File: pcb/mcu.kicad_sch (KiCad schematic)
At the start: 3 parts

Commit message: more mcu
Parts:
- added C? (x3): C, symbol Device:C
- added J?: pin_headers, symbol Carl_symboler:pin_headers
- added Y?: Crystal_GND24, symbol Device:Crystal_GND24
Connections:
- net GND: now also U?.B10 (USB_VREGI), U?.B8 (USB_VBUS), C?.2, C?.2, C?.2, Y?.2, Y?.4
- net +3.3V: now reaches U?.K8 (AVDD_2)
- net +3.3V: now also U?.K9 (AVDD_1), U?.L10 (AVDD_0)
- net at U?.L8 (PB13): now also C?.1, Y?.3
- net at U?.L9 (PB14): now also C?.1, Y?.1
- net må vi spesifisere noe her?: now reaches U?.F11 (DECOUPLE)
- net må vi spesifisere noe her?: now also C?.1

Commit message: idk
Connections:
- net +3.3V: now also U?.D5 (IOVDD_6), U?.D7 (IOVDD_5), U?.G4 (IOVDD_0), U?.G8 (IOVDD_4), U?.H7 (IOVDD_3), U?.L4 (IOVDD_1)
- no-connect marks 9 -> 10
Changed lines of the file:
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@@
   (junction (at 137.16 74.93) (diameter 0) (color 0 0 0 0)
   )
+  (junction (at 113.03 119.38) (diameter 0) (color 0 0 0 0)
+  )
   (junction (at 137.16 73.66) (diameter 0) (color 0 0 0 0)
   )
+  (junction (at 179.07 62.23) (diameter 0) (color 0 0 0 0)
+  )
   (junction (at 247.65 72.39) (diameter 0) (color 0 0 0 0)
   )
@@
   (junction (at 247.65 69.85) (diameter 0) (color 0 0 0 0)
   )
+  (junction (at 179.07 59.69) (diameter 0) (color 0 0 0 0)
+  )
+  (junction (at 173.99 48.26) (diameter 0) (color 0 0 0 0)
+  )
   (junction (at 38.1 96.52) (diameter 0) (color 0 0 0 0)
   )
   (junction (at 137.16 68.58) (diameter 0) (color 0 0 0 0)
+  )
+  (junction (at 110.49 58.42) (diameter 0) (color 0 0 0 0)
+  )
+  (junction (at 110.49 48.26) (diameter 0) (color 0 0 0 0)
   )
   (no_connect (at 152.4 69.85))
@@
   (no_connect (at 142.24 69.85))
   (no_connect (at 152.4 73.66))
+  (no_connect (at 44.45 104.14))
+  (bus_entry (at 214.63 99.06) (size 2.54 2.54)
+    (stroke (width 0) (type default) (color 0 0 0 0))
+  )
   (wire (pts (xy 247.65 72.39) (xy 247.65 105.41))
     (stroke (width 0) (type default) (color 0 0 0 0))
@@
     (stroke (width 0) (type default) (color 0 0 0 0))
   )
+  (wire (pts (xy 179.07 62.23) (xy 179.07 59.69))
+    (stroke (width 0) (type default) (color 0 0 0 0))
+  )
+  (wire (pts (xy 110.49 58.42) (xy 110.49 48.26))
+    (stroke (width 0) (type default) (color 0 0 0 0))
+  )
   (wire (pts (xy 44.45 127) (xy 36.83 127))
     (stroke (width 0) (type default) (color 0 0 0 0))
@@
     (stroke (width 0) (type default) (color 0 0 0 0))
   )
+  (wire (pts (xy 179.07 59.69) (xy 186.69 59.69))
+    (stroke (width 0) (type default) (color 0 0 0 0))
+  )
   (wire (pts (xy 105.41 66.04) (xy 133.35 66.04))
     (stroke (width 0) (type default) (color 0 0 0 0))
@@
     (stroke (width 0) (type default) (color 0 0 0 0))
   )
+  (wire (pts (xy 179.07 90.17) (xy 179.07 62.23))
+    (stroke (width 0) (type default) (color 0 0 0 0))
+  )
   (wire (pts (xy 127 88.9) (xy 127 49.53))
     (stroke (width 0) (type default) (color 0 0 0 0))
@@
     (stroke (width 0) (type default) (color 0 0 0 0))
   )
+  (wire (pts (xy 243.84 36.83) (xy 173.99 36.83))
+    (stroke (width 0) (type default) (color 0 0 0 0))
+  )
   (wire (pts (xy 237.49 105.41) (xy 247.65 105.41))
     (stroke (width 0) (type default) (color 0 0 0 0))
@@
     (stroke (width 0) (type default) (color 0 0 0 0))
   )
+  (wire (pts (xy 119.38 119.38) (xy 119.38 116.84))
+    (stroke (width 0) (type default) (color 0 0 0 0))
+  )
   (wire (pts (xy 137.16 72.39) (xy 142.24 72.39))
     (stroke (width 0) (type default) (color 0 0 0 0))
@@
     (stroke (width 0) (type default) (color 0 0 0 0))
   )
+  (wire (pts (xy 179.07 59.69) (xy 179.07 48.26))
+    (stroke (width 0) (type default) (color 0 0 0 0))
+  )
   (wire (pts (xy 264.16 95.25) (xy 273.05 95.25))
     (stroke (width 0) (type default) (color 0 0 0 0))
@@
     (stroke (width 0) (type default) (color 0 0 0 0))
   )
+  (wire (pts (xy 186.69 90.17) (xy 179.07 90.17))
+    (stroke (width 0) (type default) (color 0 0 0 0))
+  )
   (wire (pts (xy 156.21 146.05) (xy 156.21 66.04))
     (stroke (width 0) (type default) (color 0 0 0 0))
@@
     (stroke (width 0) (type default) (color 0 0 0 0))
   )
+  (wire (pts (xy 110.49 48.26) (xy 110.49 45.72))
+    (stroke (width 0) (type default) (color 0 0 0 0))
+  )
   (wire (pts (xy 105.41 88.9) (xy 127 88.9))
     (stroke (width 0) (type default) (color 0 0 0 0))
@@
     (stroke (width 0) (type default) (color 0 0 0 0))
   )
+  (wire (pts (xy 105.41 58.42) (xy 110.49 58.42))
+    (stroke (width 0) (type default) (color 0 0 0 0))
+  )
+  (wire (pts (xy 105.41 63.5) (xy 110.49 63.5))
+    (stroke (width 0) (type default) (color 0 0 0 0))
+  )
+  (wire (pts (xy 243.84 90.17) (xy 243.84 36.83))
+    (stroke (width 0) (type default) (color 0 0 0 0))
+  )
   (wire (pts (xy 44.45 101.6) (xy 38.1 101.6))
     (stroke (width 0) (type default) (color 0 0 0 0))
   )
+  (wire (pts (xy 179.07 62.23) (xy 186.69 62.23))
+    (stroke (width 0) (type default) (color 0 0 0 0))
+  )
   (wire (pts (xy 273.05 95.25) (xy 273.05 73.66))
     (stroke (width 0) (type default) (color 0 0 0 0))
@@
     (stroke (width 0) (type default) (color 0 0 0 0))
   )
+  (wire (pts (xy 237.49 90.17) (xy 243.84 90.17))
+    (stroke (width 0) (type default) (color 0 0 0 0))
+  )
   (wire (pts (xy 137.16 64.77) (xy 142.24 64.77))
     (stroke (width 0) (type default) (color 0 0 0 0))
@@
     (stroke (width 0) (type default) (color 0 0 0 0))
   )
+  (wire (pts (xy 173.99 48.26) (xy 110.49 48.26))
+    (stroke (width 0) (type default) (color 0 0 0 0))
+  )
   (wire (pts (xy 242.57 34.29) (xy 242.57 64.77))
     (stroke (width 0) (type default) (color 0 0 0 0))
@@
     (stroke (width 0) (type default) (color 0 0 0 0))
   )
+  (wire (pts (xy 173.99 36.83) (xy 173.99 48.26))
+    (stroke (width 0) (type default) (color 0 0 0 0))
+  )
+  (wire (pts (xy 110.49 63.5) (xy 110.49 58.42))
+    (stroke (width 0) (type default) (color 0 0 0 0))
+  )
   (wire (pts (xy 133.35 66.04) (xy 133.35 50.8))
     (stroke (width 0) (type default) (color 0 0 0 0))
@@
     (stroke (width 0) (type default) (color 0 0 0 0))
   )
+  (wire (pts (xy 179.07 48.26) (xy 173.99 48.26))
+    (stroke (width 0) (type default) (color 0 0 0 0))
+  )
   (wire (pts (xy 273.05 73.66) (xy 241.3 73.66))
     (stroke (width 0) (type default) (color 0 0 0 0))
@@
   )
   (wire (pts (xy 154.94 49.53) (xy 154.94 64.77))
+    (stroke (width 0) (type default) (color 0 0 0 0))
+  )
+  (wire (pts (xy 113.03 119.38) (xy 119.38 119.38))
     (stroke (width 0) (type default) (color 0 0 0 0))
   )
@@
     )
     (property "Datasheet" "" (id 3) (at 247.65 68.58 0)
+      (effects (font (size 1.27 1.27)) hide)
+    )
+    (pin "1")
+  )
+  (symbol (lib_id "power:PWR_FLAG") (at 119.38 116.84 0) (unit 1)
+    (in_bom yes) (on_board yes) (fields_autoplaced)
+    (property "Reference" "#FLG?" (id 0) (at 119.38 114.935 0)
+      (effects (font (size 1.27 1.27)) hide)
+    )
+    (property "Value" "" (id 1) (at 119.38 111.76 0))
+    (property "Footprint" "" (id 2) (at 119.38 116.84 0)
+      (effects (font (size 1.27 1.27)) hide)
+    )
+    (property "Datasheet" "~" (id 3) (at 119.38 116.84 0)
       (effects (font (size 1.27 1.27)) hide)
     )
@@
       (effects (font (size 1.27 1.27)) hide)
     )
+    (pin "1")
+  )
+  (symbol (lib_id "power:+3.3V") (at 110.49 45.72 0) (unit 1)
+    (in_bom yes) (on_board yes) (fields_autoplaced)
+    (property "Reference" "#PWR?" (id 0) (at 110.49 49.53 0)
+      (effects (font (size 1.27 1.27)) hide)
+    )
+    (property "Value" "" (id 1) (at 110.49 40.64 0))
+    (property "Footprint" "" (id 2) (at 110.49 45.72 0)
+      (effects (font (size 1.27 1.27)) hide)
+    )
+    (property "Datasheet" "" (id 3) (at 110.49 45.72 0)
+      (effects (font (size 1.27 1.27)) hide)
+    )

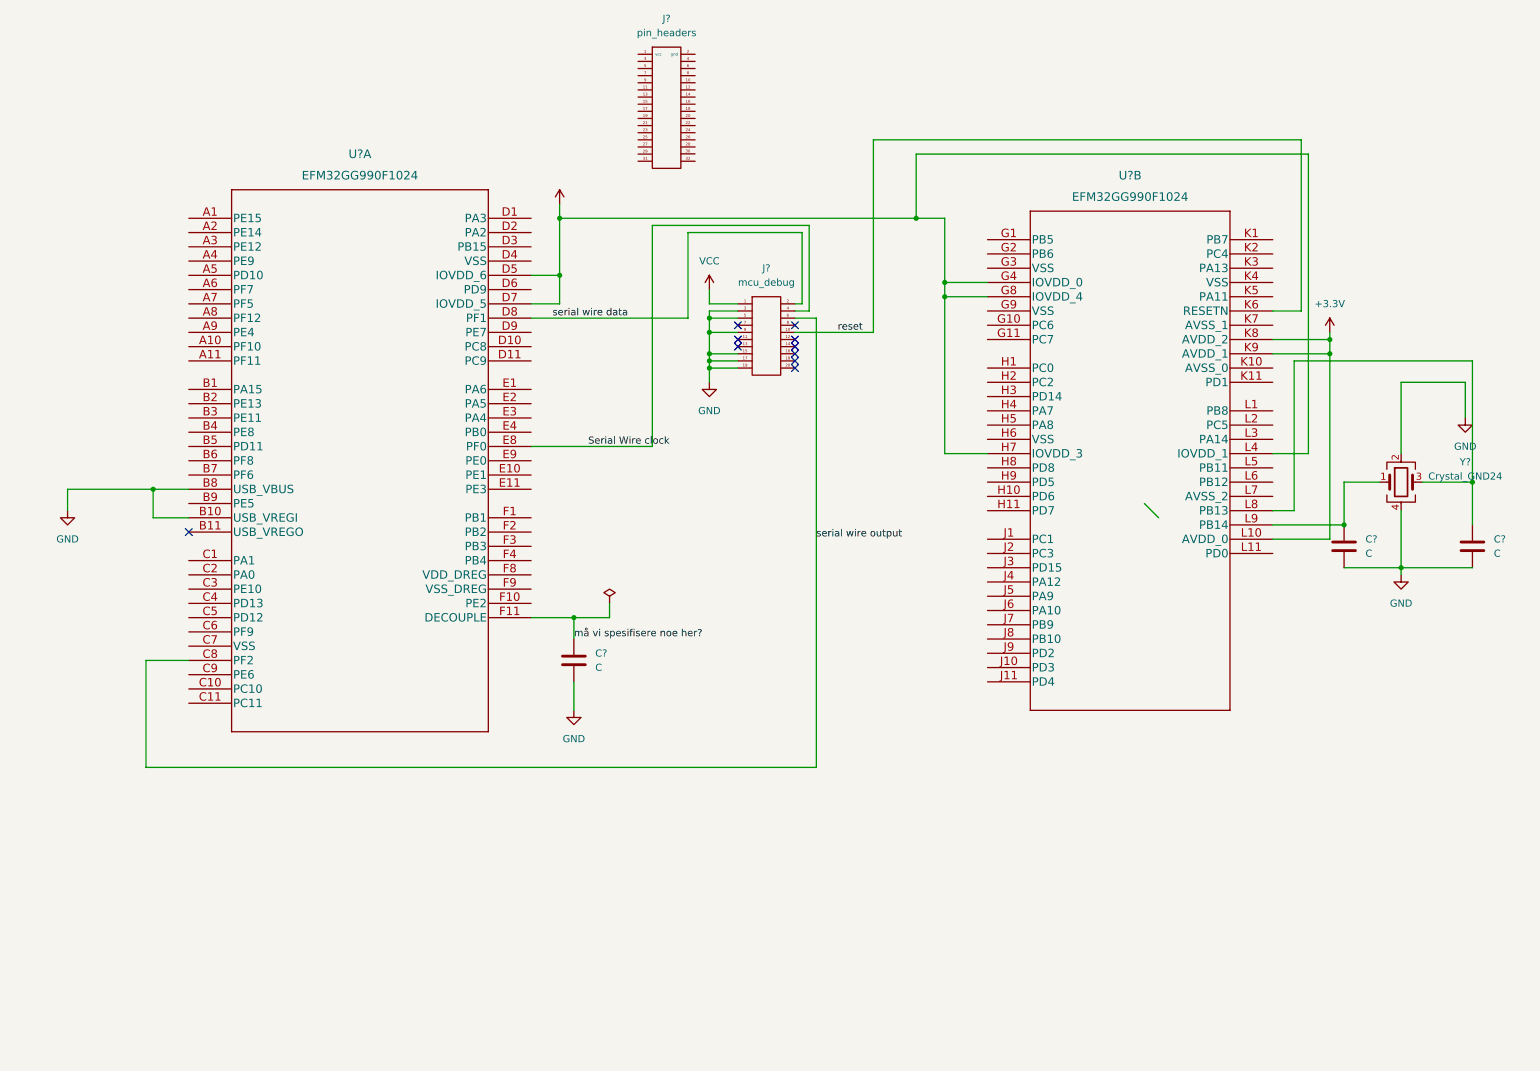
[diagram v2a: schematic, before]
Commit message: add global labels and footprint
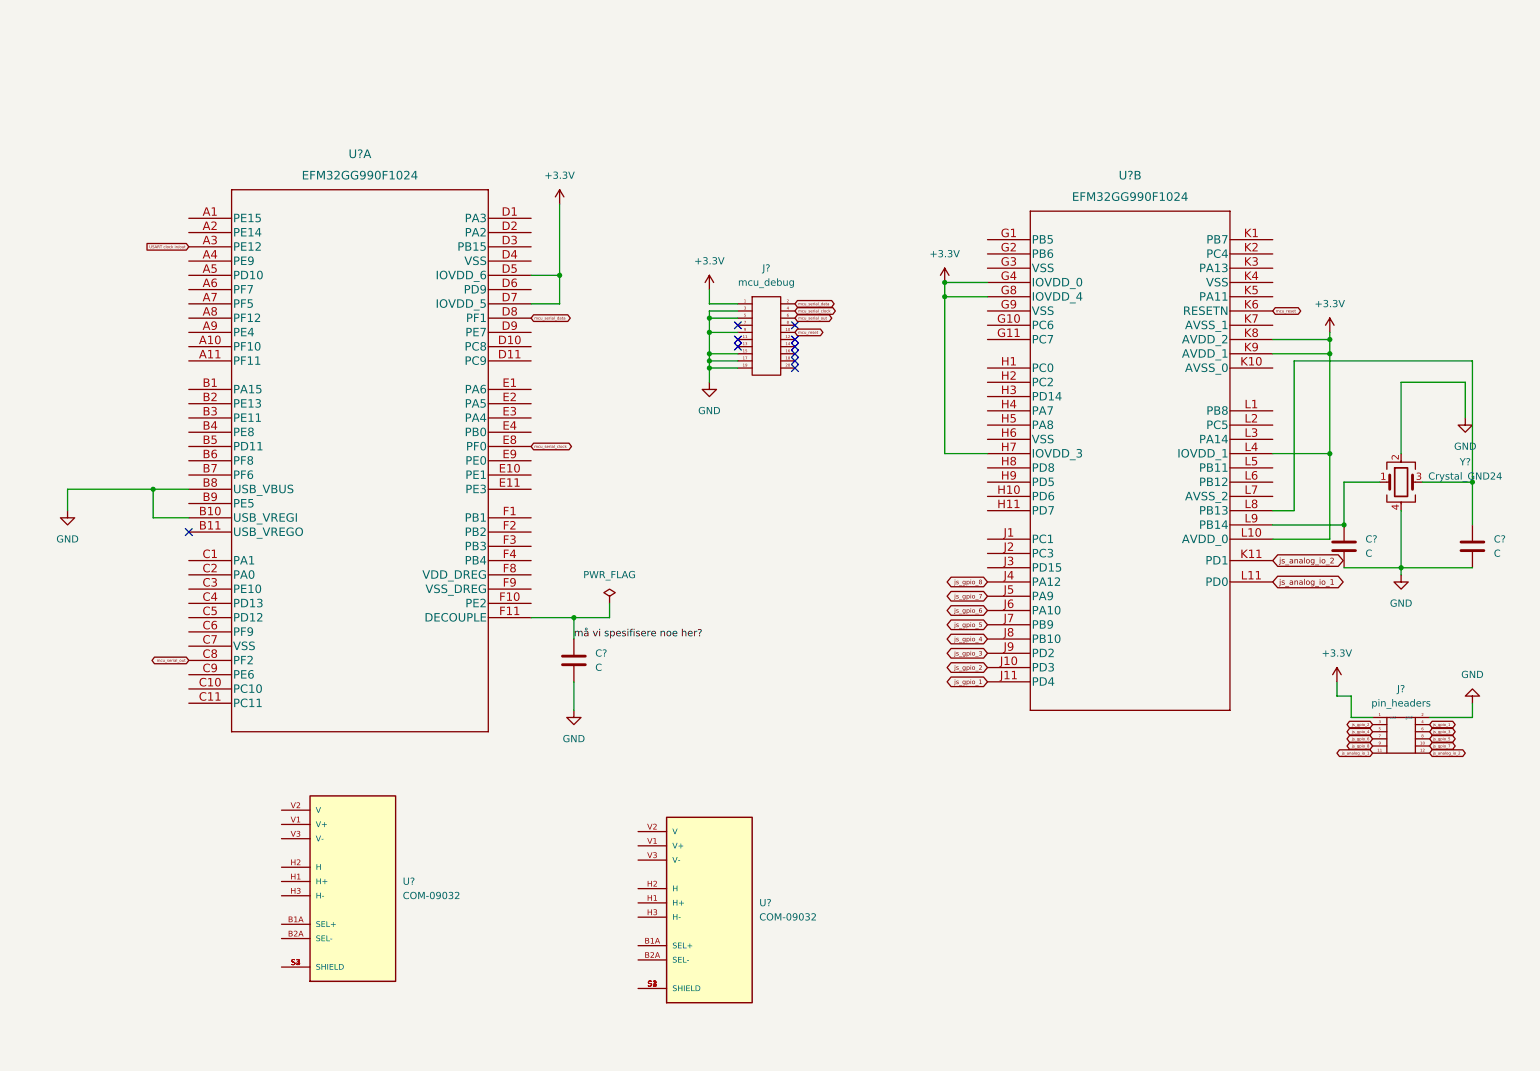
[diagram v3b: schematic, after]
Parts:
- removed J?: pin_headers, symbol Carl_symboler:pin_headers
- added J?: pin_headers, symbol Carl_symboler:pin_headers
- added U? (x2): COM-09032, mcu_kicad:XDCR_COM-09032, symbol COM-09032:COM-09032
- U? (x2): footprint BGA112 -> mcu_kicad:EFM32GG990F1024
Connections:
- net VCC is gone; now on net +3.3V: J?.1
- net +3.3V: now also J?.1 (vcc)
- net GND: now also J?.2 (gnd)
- net js_gpio_2: now reaches U?.J10 (PD3)
- net js_gpio_2: now also J?.3
- net js_gpio_1: now reaches U?.J11 (PD4)
- net js_gpio_1: now also J?.4
- net js_gpio_8: now reaches U?.J4 (PA12)
- net js_gpio_8: now also J?.9
- net js_gpio_7: now reaches U?.J5 (PA9)
- net js_gpio_7: now also J?.10
- net js_gpio_6: now reaches U?.J6 (PA10)
- net js_gpio_6: now also J?.7
- net js_gpio_5: now reaches U?.J7 (PB9)
- net js_gpio_5: now also J?.8
- net js_gpio_4: now reaches U?.J8 (PB10)
- net js_gpio_4: now also J?.5
- net js_gpio_3: now reaches U?.J9 (PD2)
- net js_gpio_3: now also J?.6
- net js_analog_io_2: now reaches U?.K11 (PD1)
- net js_analog_io_2: now also J?.12
- net js_analog_io_1: now reaches U?.L11 (PD0)
- net js_analog_io_1: now also J?.11
- net USART clock in/out: now reaches U?.A3 (PE12)
- net Serial Wire clock renamed mcu_serial_clock
- net reset renamed mcu_reset
- net serial wire data renamed mcu_serial_data
- net serial wire output renamed mcu_serial_out
- new net: U?.S1 (SHIELD), U?.S2 (SHIELD), U?.S3 (SHIELD), U?.S4 (SHIELD) (x2)

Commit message: io_controller_inputs on mcu
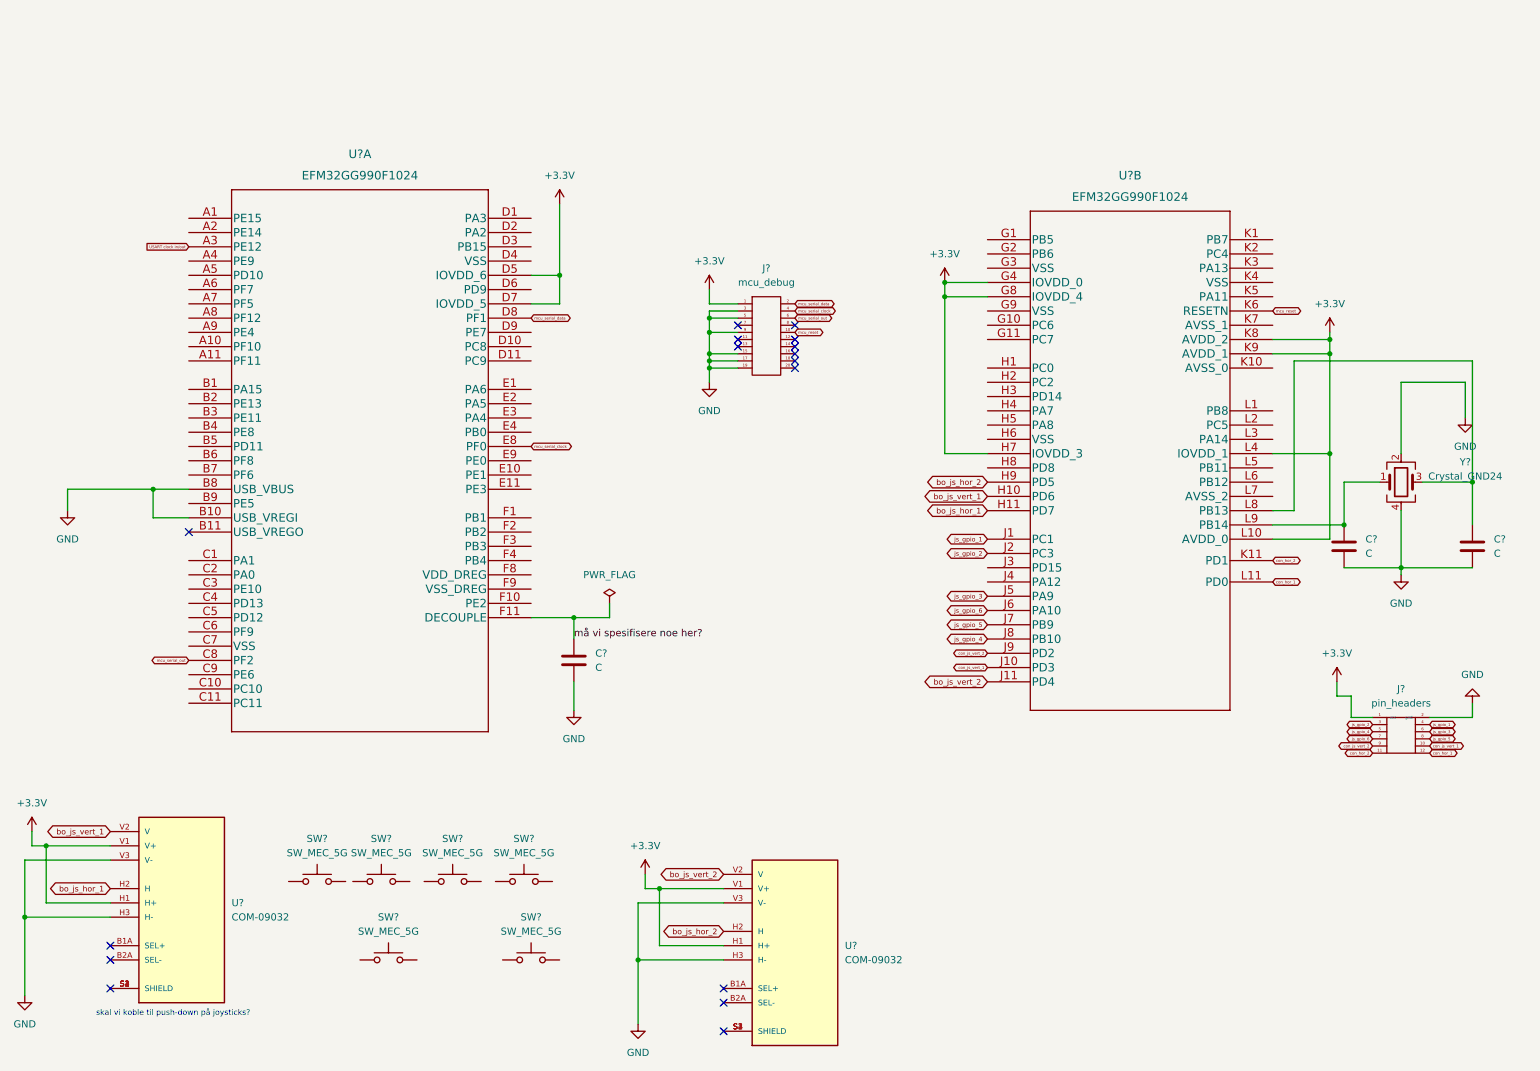
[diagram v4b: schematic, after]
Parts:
- removed U?: COM-09032, mcu_kicad:XDCR_COM-09032, symbol COM-09032:COM-09032
- added SW? (x6): SW_MEC_5G, symbol Switch:SW_MEC_5G
- added U?: COM-09032, mcu_kicad:XDCR_COM-09032, symbol COM-09032:COM-09032
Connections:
- net +3.3V: now also U?.H1 (H+), U?.V1 (V+), U?.H1 (H+), U?.V1 (V+)
- net GND: now also U?.H3 (H-), U?.V3 (V-), U?.H3 (H-), U?.V3 (V-)
- net js_gpio_1: now also U?.J1 (PC1); no longer U?.J11 (PD4)
- net js_gpio_2: now also U?.J2 (PC3); no longer U?.J10 (PD3)
- net js_gpio_3: now also U?.J5 (PA9); no longer U?.J9 (PD2)
- net bo_js_hor_1: now reaches U?.H2 (H)
- net bo_js_hor_1: now also U?.H11 (PD7)
- net bo_js_vert_1: now reaches U?.V2 (V)
- net bo_js_vert_1: now also U?.H10 (PD6)
- net bo_js_hor_2: now reaches U?.H9 (PD5)
- net bo_js_hor_2: now also U?.H2 (H)
- net js_analog_io_1 renamed con_hor_1
- net con_hor_1: now also J?.12; no longer J?.11
- net js_analog_io_2 renamed con_hor_2
- net con_hor_2: now also J?.11; no longer J?.12
- net js_gpio_7 renamed con_js_vert_1
- net con_js_vert_1: now also U?.J10 (PD3); no longer U?.J5 (PA9)
- net js_gpio_8: no longer names the net of U?.J4 (PA12)
- net js_gpio_8: no longer J?.9
- new net: SW?.1 (A), SW?.2 (A) (x6)
- new net: SW?.3 (B), SW?.4 (B) (x6)
- new net: U?.S1 (SHIELD), U?.S2 (SHIELD), U?.S3 (SHIELD), U?.S4 (SHIELD)
- new net bo_js_vert_2: U?.J11 (PD4), U?.V2 (V)
- new net con_js_vert_2: J?.9, U?.J9 (PD2)
- no-connect marks 10 -> 16
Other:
- note added: "skal vi koble til push-down på joysticks?"
- moved on the sheet: U?

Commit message: finish onboard controller
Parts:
- removed SW? (x6): SW_MEC_5G, symbol Switch:SW_MEC_5G
- removed U? (x2): COM-09032, mcu_kicad:XDCR_COM-09032, symbol COM-09032:COM-09032
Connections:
- net GND: no longer C?.2
- net con_js_vert_1: now also J?.11; no longer J?.10
- net bo_js_button_1: now reaches U?.A11 (PF11)
- net bo_button_1: now reaches U?.B1 (PA15)
- net bo_button_2: now reaches U?.B2 (PE13)
- net bo_button_3: now reaches U?.B3 (PE11)
- net bo_button_4: now reaches U?.B4 (PE8)
- net bo_button_5: now reaches U?.B5 (PD11)
- net bo_button_6: now reaches U?.B6 (PF8)
- net con_hor_2 renamed con_js_button
- net con_js_button: now also J?.9; no longer J?.11
- net con_js_vert_2: no longer names the net of U?.J9 (PD2)
- net con_js_vert_2: no longer J?.9
- no-connect marks 16 -> 11
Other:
- added sheet onboard_controller (onboard_controller.kicad_sch)
- note removed: "skal vi koble til push-down på joysticks?"

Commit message: add externall controller
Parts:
- removed J?: pin_headers, symbol Carl_symboler:pin_headers
- added J?: 1658525-9, 1658525-9-ribbon:TE_1658525-9, symbol 1658525-9:1658525-9
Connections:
- net +3.3V: now also J?.1
- net GND: now also J?.2
- net con_hor_1: now also J?.12
- net con_js_button: now also J?.9
- net con_js_vert_1: now also J?.11
- net js_gpio_1: now also J?.4
- net js_gpio_2: now also J?.3
- net js_gpio_3: now also J?.6
- net js_gpio_4: now also J?.5
- net js_gpio_5: now also J?.8
- net js_gpio_6: now also J?.7
- no-connect marks 11 -> 19
